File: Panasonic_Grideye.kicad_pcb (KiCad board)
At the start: 2 copper layers, 20.8 x 25.4 mm, 9 parts, among them P1 CONN_01X05, U1 GridEye

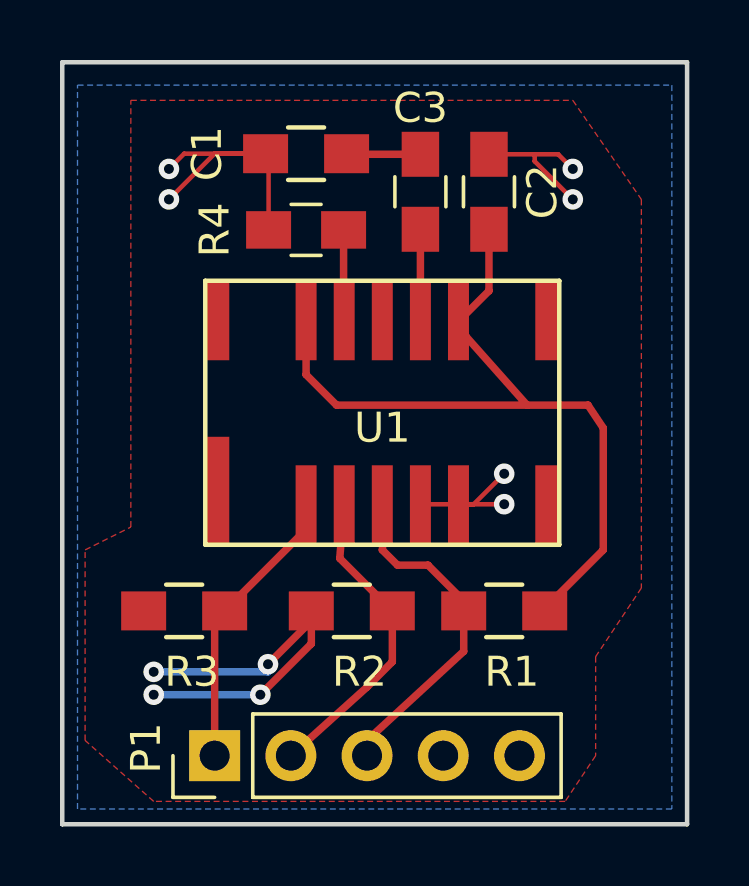
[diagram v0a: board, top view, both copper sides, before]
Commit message: Updating Changes Made to Board Files
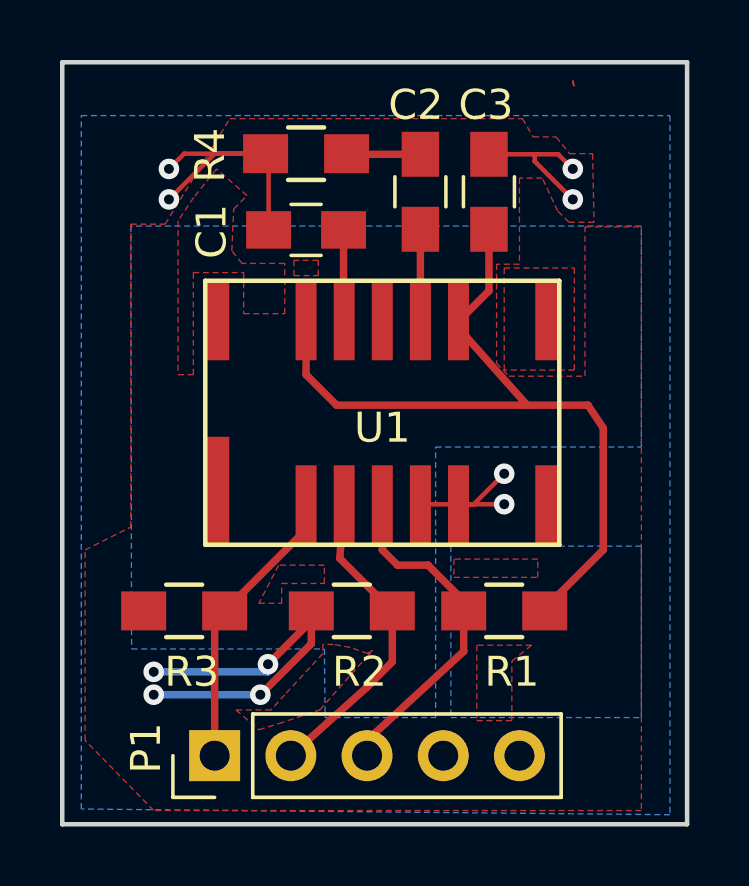
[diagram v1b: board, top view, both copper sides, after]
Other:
- board text added: "V1.1"
- board text removed: "V1.0"
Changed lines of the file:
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@@
     (links 20)
     (no_connects 0)
-    (area 142.164999 98.984999 163.143001 124.535001)
+    (area 142.164999 98.984999 163.143001 127.159733)
     (thickness 1.6)
     (drawings 12)
@@
     (34 B.Paste user hide)
     (35 F.Paste user hide)
-    (36 B.SilkS user)
-    (37 F.SilkS user hide)
-    (38 B.Mask user)
+    (36 B.SilkS user hide)
+    (37 F.SilkS user)
+    (38 B.Mask user hide)
     (39 F.Mask user)
-    (44 Edge.Cuts user)
+    (44 Edge.Cuts user hide)
   )
   (setup
@@
     (pad_drill 0.762)
     (pad_to_mask_clearance 0.2)
-    (aux_axis_origin 0 0)
-    (visible_elements 7FFEF7FF)
+    (aux_axis_origin 161.544 104.521)
+    (visible_elements 7FFF5229)
     (pcbplotparams
       (layerselection 0x00030_80000001)
@@
     (tags "capacitor 0805")
     (attr smd)
-    (fp_text reference C1 (at 3.302 2.54 450) (layer F.SilkS)
-      (effects (font (size 1 1) (thickness 0.15)))
-    )
-    (fp_text value 1.5uF (at 0 2.1 180) (layer F.Fab)
+    (fp_text reference C1 (at 3.1496 -0.0508 450) (layer F.SilkS)
+      (effects (font (size 1 1) (thickness 0.15)))
+    )
+    (fp_text value 1.5uF (at 0.2032 -1.016 180) (layer F.Fab)
       (effects (font (size 1 1) (thickness 0.15)))
     )
@@
     (tags "capacitor 0805")
     (attr smd)
-    (fp_text reference C2 (at 0 4.064 270) (layer F.SilkS)
-      (effects (font (size 1 1) (thickness 0.15)))
-    )
-    (fp_text value 1uF (at 0 2.1 90) (layer F.Fab)
+    (fp_text reference C2 (at 2.8956 -0.1524 360) (layer F.SilkS)
+      (effects (font (size 1 1) (thickness 0.15)))
+    )
+    (fp_text value 1uF (at 0.1524 -1.6256 90) (layer F.Fab)
       (effects (font (size 1 1) (thickness 0.15)))
     )
@@
     (tags "capacitor 0805")
     (attr smd)
-    (fp_text reference C3 (at 2.794 -2.286 180) (layer F.SilkS)
+    (fp_text reference C3 (at 2.8956 -0.1016 180) (layer F.SilkS)
       (effects (font (size 1 1) (thickness 0.15)))
     )
@@
     (tags "resistor 0805")
     (attr smd)
-    (fp_text reference R4 (at 3.048 -2.54 270) (layer F.SilkS)
-      (effects (font (size 1 1) (thickness 0.15)))
-    )
-    (fp_text value 10 (at 0 2.1 180) (layer F.Fab)
+    (fp_text reference R4 (at 3.2004 -0.0508 270) (layer F.SilkS)
+      (effects (font (size 1 1) (thickness 0.15)))
+    )
+    (fp_text value 10 (at 0.3556 1.524 180) (layer F.Fab)
       (effects (font (size 1 1) (thickness 0.15)))
     )
@@
     (effects (font (size 1 1) (thickness 0.2)) (justify mirror))
   )
-  (gr_text "V1.0 " (at 162.052 119.38 270) (layer B.SilkS)
+  (gr_text V1.1 (at 162.052 119.38 270) (layer B.SilkS)
     (effects (font (size 1 1) (thickness 0.2)) (justify mirror))
   )
@@
     (polygon
       (pts
-        (xy 142.748 99.822) (xy 162.56 99.822) (xy 162.56 123.952) (xy 142.748 123.952) (xy 142.748 101.854)
+        (xy 162.4965 124.1425) (xy 142.875 123.952) (xy 142.875 100.838) (xy 162.4965 100.838)
+      )
+    )
+    (polygon
+      (pts        (xy 155.194 115.189) (xy 155.194 120.904) (xy 161.544 120.904) (xy 161.544 115.189)
+      )
+    )
+    (polygon
+      (pts        (xy 144.526 104.521) (xy 144.5514 118.618) (xy 150.9776 118.618) (xy 151.003 120.904) (xy 154.686 120.904)
+        (xy 154.686 111.887) (xy 161.544 111.887) (xy 161.544 104.521)
       )
     )
@@
     (polygon
       (pts
-        (xy 159.004 123.698) (xy 145.288 123.698) (xy 143.002 121.666) (xy 143.002 115.316) (xy 144.526 114.554)
-        (xy 144.526 100.33) (xy 159.258 100.33) (xy 161.544 103.632) (xy 161.544 116.586) (xy 160.02 118.872)
-        (xy 160.02 122.174)
-      )
-    )
+        (xy 157.9372 101.5492) (xy 158.6992 101.5492) (xy 159.1564 102.108) (xy 159.9184 102.108) (xy 159.966025 104.394)
+        (xy 159.131 104.394) (xy 158.75 104.013) (xy 158.242 102.9208) (xy 157.48 102.9208) (xy 157.48 105.791)
+        (xy 156.718 105.791) (xy 156.718 109.093) (xy 157.1244 109.5248) (xy 159.6644 109.5248) (xy 159.6644 104.5464)
+        (xy 161.544 104.5464) (xy 161.544 124.0028) (xy 145.288 124.0028) (xy 143.002 121.666) (xy 143.002 115.316)
+        (xy 144.526 114.554) (xy 144.526 104.4575) (xy 145.669 104.4575) (xy 147.828 100.9396) (xy 157.5816 100.9396)
+      )
+    )
+    (polygon
+      (pts        (xy 150.9268 118.4656) (xy 150.9268 118.7704) (xy 149.6568 120.142) (xy 149.1996 120.65) (xy 148.0312 120.65)
+        (xy 148.7932 121.3104) (xy 149.4536 121.1072) (xy 150.8252 120.65) (xy 152.379637 118.885504) (xy 152.601996 118.668704)
+        (xy 152.572693 118.666359) (xy 152.4254 118.7704) (xy 151.8412 118.5672) (xy 151.2824 118.4656)
+      )
+    )
+    (polygon
+      (pts        (xy 156.0576 118.491) (xy 156.0576 121.0056) (xy 157.226 121.0056) (xy 157.226 119.0244) (xy 157.8864 118.491)
+      )
+    )
+    (polygon
+      (pts        (xy 149.4536 115.824) (xy 148.7932 117.094) (xy 149.5552 117.094) (xy 149.5552 116.4336) (xy 150.9776 116.4336)
+        (xy 150.9776 115.824)
+      )
+    )
+    (polygon
+      (pts        (xy 155.2956 115.6208) (xy 155.2956 116.2304) (xy 158.0896 116.2304) (xy 158.0896 115.6208)
+      )
+    )
+    (polygon
+      (pts        (xy 146.6215 103.5685) (xy 146.1008 104.3432) (xy 146.1008 109.474) (xy 146.6088 109.474) (xy 146.6088 106.0704)
+        (xy 148.2852 106.0704) (xy 148.2852 107.442) (xy 149.6568 107.442) (xy 149.6568 105.7656) (xy 148.2344 105.7656)
+        (xy 147.8915 105.3465) (xy 147.955 103.9495) (xy 148.3995 103.505) (xy 147.3835 102.616)
+      )
+    )
+    (polygon
+      (pts        (xy 149.9616 105.664) (xy 149.9616 106.172) (xy 150.7744 106.172) (xy 150.7744 105.664)
+      )
+    )
+  )
+  (zone (net 5) (net_name VDD) (layer F.Cu) (hatch edge 0.508)
+    (connect_pads (clearance 0.508))
+    (min_thickness 0.254)
+    (fill yes (arc_segments 16) (thermal_gap 0.508) (thermal_bridge_width 0.508))
+    (polygon
+      (pts
+        (xy 159.3088 109.3216) (xy 156.972 109.3216) (xy 156.972 105.918) (xy 159.3088 105.918)
+      )
+    )
+  )
+  (zone (net 5) (net_name VDD) (layer F.Cu) (hatch edge 0.508)
+    (connect_pads (clearance 0.508))
+    (min_thickness 0.254)
+    (fill yes (arc_segments 16) (thermal_gap 0.508) (thermal_bridge_width 0.508))
+    (polygon
+      (pts
+        (xy 159.309371 99.85796) (xy 159.258 99.7712) (xy 159.258 99.6696)
+      )
+    )
